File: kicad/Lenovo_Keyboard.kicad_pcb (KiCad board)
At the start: 2 copper layers, 100 x 37 mm, 14 parts, among them J1 Conn_01x34_Pin, J2 Conn_01x04_Socket, J3 Conn_01x04_Socket

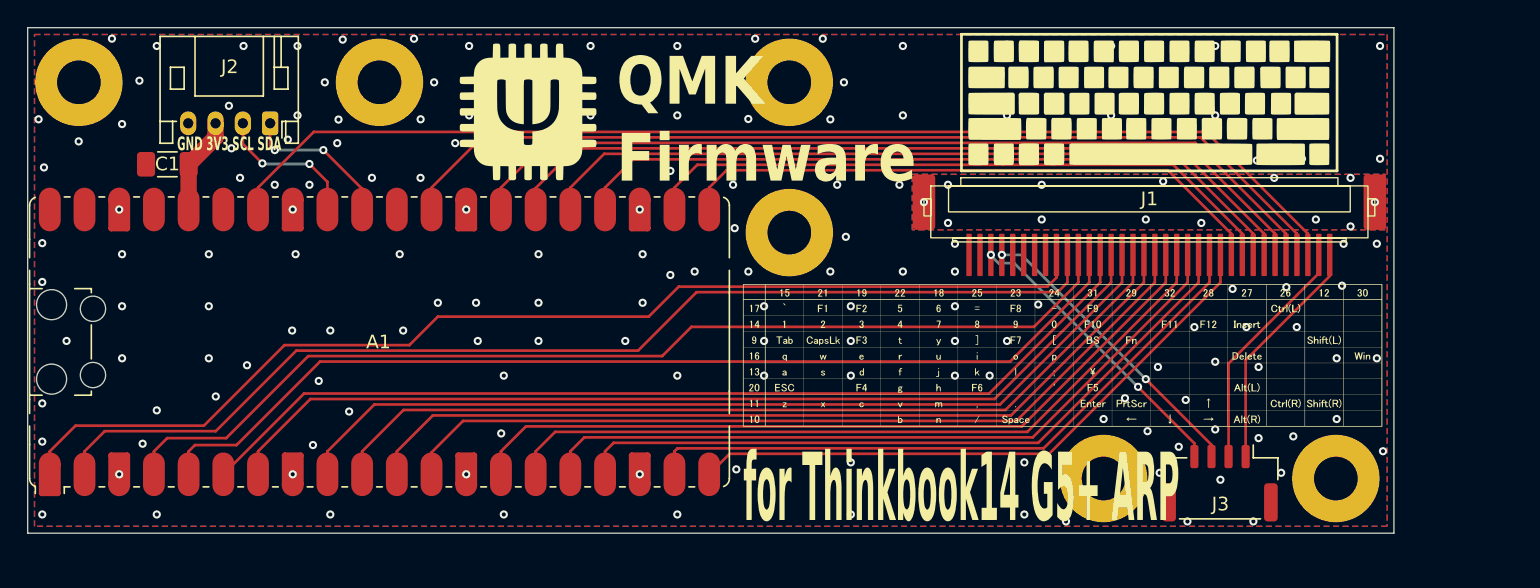
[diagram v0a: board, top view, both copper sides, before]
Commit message: CapsLk/Escape LED support
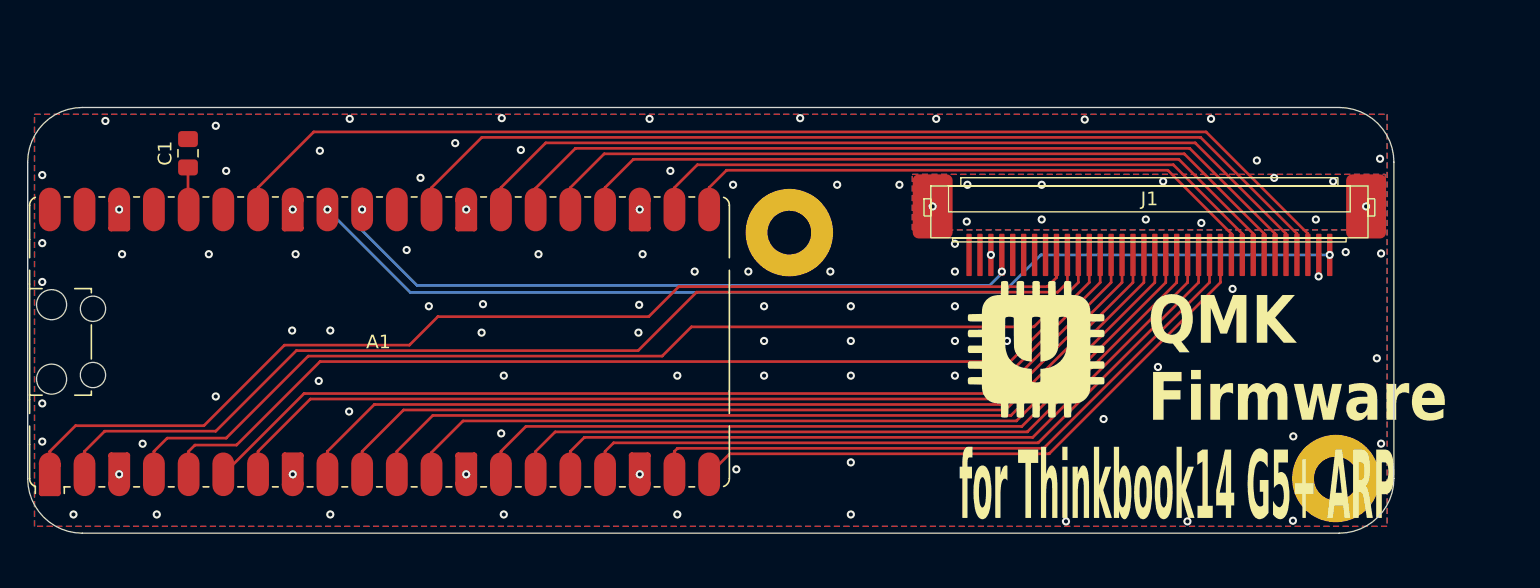
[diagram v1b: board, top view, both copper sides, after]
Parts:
- removed the G*** at (212.3, 57.5)
- removed the G*** at (206.0, 75.9)
- removed J2: Conn_01x04_Socket, Connector_JST:JST_PH_S4B-PH-K_1x04_P2.00mm_Horizontal
- removed J3: Conn_01x04_Socket, Connector_JST:JST_GH_BM04B-GHS-TBT_1x04-1MP_P1.25mm_Vertical
- removed the REF** at (209.0, 85.0)
- removed the REF** at (186.0, 56.0)
- removed the REF** at (134.0, 56.0)
- removed the REF** at (156.0, 56.0)
- C1: value 10uF -> 0.1uF; footprint Capacitor_SMD:C_1206_3216Metric_Pad1.33x1.80mm_HandSolder -> Capacitor_SMD:C_0805_2012Metric_Pad1.18x1.45mm_HandSolder
- moved G*** 41.0 mm to (204.1, 75.5)
- moved C1 1.71 mm to (142.0, 61.2), turned to 90 degrees
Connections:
- A1 pad 31: SDA -> LED_CAPSLK
- A1 pad 32: SCL -> LED_ESC
- J1 pad 3: PFC_N0 -> GND
- J1 pad 33: PFC_N2 -> GND
- J1 pad 34: PFC_N3 -> LED_ESC
- J1 pad 4: PFC_N1 -> LED_CAPSLK
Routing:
- net LED_ESC: track 0.00 -> 77.0 mm, vias 0 -> 2
- net LED_CAPSLK: track 0.00 -> 52.0 mm, vias 0 -> 2
- net PFC_N1: track 22.0 -> 0.00 mm, vias 2 -> 0
- net PFC_N0: track 21.6 -> 0.00 mm, vias 2 -> 0
- net PFC_N2: track 17.5 -> 0.00 mm
- net PFC_N3: track 17.3 -> 0.00 mm
- net SDA: track 11.2 -> 0.00 mm, vias 2 -> 0
- net SCL: track 10.9 -> 0.00 mm, vias 2 -> 0
- net +3V3: track 7.13 -> 3.10 mm
- net GND: track 0.00 -> 2.03 mm, vias 160 -> 91
- net Earth: vias 13 -> 12
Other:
- board size 100 x 37 mm -> 100 x 31.2 mm
- board text removed: "GND 3V3 SCL SDA"
